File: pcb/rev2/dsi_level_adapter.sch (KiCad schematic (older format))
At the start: 6 parts

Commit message: pcb wip
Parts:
- RA3: renamed from R3A1; footprint RESC1608X55N -> Resistors SMD:RESC1608X55N
- RA4: renamed from R4A1; footprint RESC1608X55N -> Resistors SMD:RESC1608X55N
- RA5: renamed from R5A1; footprint RESC1608X55N -> Resistors SMD:RESC1608X55N
- RA51: renamed from R51A1; footprint RESC1608X55N -> Resistors SMD:RESC1608X55N; Fieldname (none) -> Value
- RA52: renamed from R52A1; footprint RESC1608X55N -> Resistors SMD:RESC1608X55N
- RA6: renamed from R6A; footprint RESC1608X55N -> Resistors SMD:RESC1608X55N

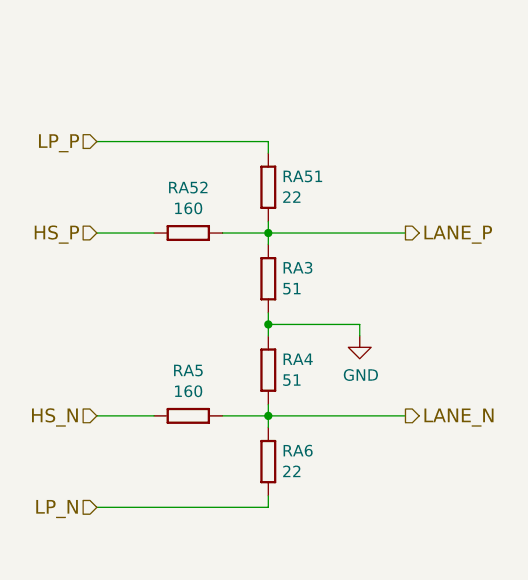
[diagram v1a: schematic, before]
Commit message: Completed port to KiCad, passes DRC+LVS. NOT MANUFACTURED.
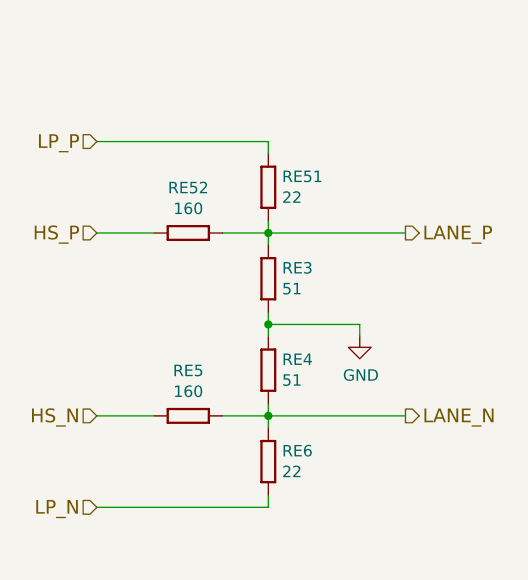
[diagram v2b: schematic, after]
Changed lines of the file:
@@
 AR Path="/598D85B4/598E1801/598DB2C0" Ref="RD52"  Part="1"
 AR Path="/598D85B4/598E2C48/598DB2C0" Ref="RE52"  Part="1"
-F 0 "RA52" H 6750 1903 50  0000 C CNN
+F 0 "RE52" H 6750 1903 50  0000 C CNN
 F 1 "R0603_160R_1%_0.1W_100PPM" H 6600 1890 60  0001 L CNN
 F 2 "Resistors SMD:RESC1608X55N" H 6600 1080 60  0001 L CNN
@@
 AR Path="/598D85B4/598E1801/598DC2CA" Ref="RD51"  Part="1"
 AR Path="/598D85B4/598E2C48/598DC2CA" Ref="RE51"  Part="1"
-F 0 "RA51" V 6904 1810 50  0000 L CNN
+F 0 "RE51" V 6904 1810 50  0000 L CNN
 F 1 "R0603_22R_1%_0.1W_100PPM" H 6800 1540 60  0001 L CNN
 F 2 "Resistors SMD:RESC1608X55N" H 6800 730 60  0001 L CNN
@@
 AR Path="/598D85B4/598E1801/598DD2C1" Ref="RD3"  Part="1"
 AR Path="/598D85B4/598E2C48/598DD2C1" Ref="RE3"  Part="1"
-F 0 "RA3" V 6904 2210 50  0000 L CNN
+F 0 "RE3" V 6904 2210 50  0000 L CNN
 F 1 "R0603_51R_1%_0.1W_100PPM" H 6800 1940 60  0001 L CNN
 F 2 "Resistors SMD:RESC1608X55N" H 6800 1130 60  0001 L CNN
@@
 AR Path="/598D85B4/598E1801/598DDA7D" Ref="RD4"  Part="1"
 AR Path="/598D85B4/598E2C48/598DDA7D" Ref="RE4"  Part="1"
-F 0 "RA4" V 6904 2610 50  0000 L CNN
+F 0 "RE4" V 6904 2610 50  0000 L CNN
 F 1 "R0603_51R_1%_0.1W_100PPM" H 6800 2340 60  0001 L CNN
 F 2 "Resistors SMD:RESC1608X55N" H 6800 1530 60  0001 L CNN
@@
 AR Path="/598D85B4/598E1801/598DDD38" Ref="RD6"  Part="1"
 AR Path="/598D85B4/598E2C48/598DDD38" Ref="RE6"  Part="1"
-F 0 "RA6" V 6904 3010 50  0000 L CNN
+F 0 "RE6" V 6904 3010 50  0000 L CNN
 F 1 "R0603_22R_1%_0.1W_100PPM" H 6800 2740 60  0001 L CNN
 F 2 "Resistors SMD:RESC1608X55N" H 6800 1930 60  0001 L CNN
@@
 AR Path="/598D85B4/598E1801/598DDDBE" Ref="RD5"  Part="1"
 AR Path="/598D85B4/598E2C48/598DDDBE" Ref="RE5"  Part="1"
-F 0 "RA5" H 6750 2703 50  0000 C CNN
+F 0 "RE5" H 6750 2703 50  0000 C CNN
 F 1 "R0603_160R_1%_0.1W_100PPM" H 6600 2690 60  0001 L CNN
 F 2 "Resistors SMD:RESC1608X55N" H 6600 1880 60  0001 L CNN

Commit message: axi4/zynq version: wip
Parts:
- RA3, RA4: symbol R0603_51R_1%_0.1W_100PPM -> dsi_shield-rescue:R0603_51R_1%_0.1W_100PPM-
- RA5, RA52: symbol R0603_160R_1%_0.1W_100PPM -> dsi_shield-rescue:R0603_160R_1%_0.1W_100PPM-
- RA51, RA6: symbol R0603_22R_1%_0.1W_100PPM -> dsi_shield-rescue:R0603_22R_1%_0.1W_100PPM-
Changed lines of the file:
@@
-EESchema Schematic File Version 2
-LIBS:Capacitors Networks THD
-LIBS:Capacitors Networks SMD
-LIBS:Capacitors THD
-LIBS:Capacitors SMD
-LIBS:Miscellaneous
-LIBS:HARWIN
-LIBS:LEMO
-LIBS:WEIDMULLER
-LIBS:FCI
-LIBS:MOLEX
-LIBS:TYCO
-LIBS:ERNI
-LIBS:MENTOR
-LIBS:SAMTEC
-LIBS:STELVIO-KONTEK COMATEL
-LIBS:AMPHENOL
-LIBS:HARTING
-LIBS:3M
-LIBS:Pads
-LIBS:Switches
-LIBS:Relays
-LIBS:Heat-Sinks
-LIBS:Fasteners & Fixings
-LIBS:Batteries
-LIBS:Fuses
-LIBS:Metal Screening Box
-LIBS:Sockets
-LIBS:Regulators
-LIBS:Transistors
-LIBS:Power Supplies
-LIBS:Analog & Interface
-LIBS:Sensors
-LIBS:Logic
-LIBS:Optocouplers
-LIBS:Standard Logic
-LIBS:DC-DC Converters
-LIBS:Operational Amplifiers
-LIBS:Crystals & Oscillators
-LIBS:Diodes
-LIBS:LEDs & Displays
-LIBS:PCB Modules
-LIBS:Bonding
-LIBS:Resistors THD
-LIBS:Potentiometers SMD
-LIBS:Thermistors And Varistors
-LIBS:Potentiometers THD
-LIBS:Resistor Networks THD
-LIBS:Resistors SMD
-LIBS:Resistor Networks SMD
-LIBS:Transformers
-LIBS:Inductors SMD
-LIBS:Inductors THD
-LIBS:Cores
-LIBS:power
-LIBS:conn
-LIBS:dsi_shield
+EESchema Schematic File Version 4
 LIBS:dsi_shield-cache
 EELAYER 26 0
@@
 $EndDescr
 $Comp
-L R0603_160R_1%_0.1W_100PPM RA52
+L dsi_shield-rescue:R0603_160R_1%_0.1W_100PPM- RA52
 U 1 1 598DB2C0
 P 6600 2100
@@
 $EndComp
 $Comp
-L R0603_22R_1%_0.1W_100PPM RA51
+L dsi_shield-rescue:R0603_22R_1%_0.1W_100PPM- RA51
 U 1 1 598DC2CA
 P 6800 1750
@@
 $EndComp
 $Comp
-L R0603_51R_1%_0.1W_100PPM RA3
+L dsi_shield-rescue:R0603_51R_1%_0.1W_100PPM- RA3
 U 1 1 598DD2C1
 P 6800 2150
@@
 Connection ~ 6800 2100
 $Comp
-L R0603_51R_1%_0.1W_100PPM RA4
+L dsi_shield-rescue:R0603_51R_1%_0.1W_100PPM- RA4
 U 1 1 598DDA7D
 P 6800 2550
@@
 	6800 2550 6800 2450
 $Comp
-L GND #PWR034
+L dsi_shield-rescue:GND- #PWR034
 U 1 1 598DDCCB
 P 7200 2550
@@
 Connection ~ 6800 2500
 $Comp
-L R0603_22R_1%_0.1W_100PPM RA6
+L dsi_shield-rescue:R0603_22R_1%_0.1W_100PPM- RA6
 U 1 1 598DDD38
 P 6800 2950
@@
 $EndComp
 $Comp
-L R0603_160R_1%_0.1W_100PPM RA5
+L dsi_shield-rescue:R0603_160R_1%_0.1W_100PPM- RA5
 U 1 1 598DDDBE
 P 6600 2900
